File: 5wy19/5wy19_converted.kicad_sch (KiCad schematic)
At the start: 0 parts

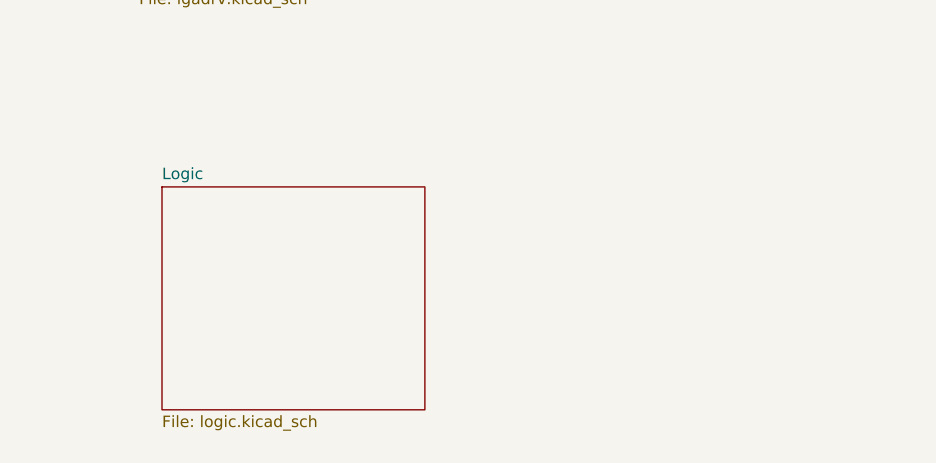
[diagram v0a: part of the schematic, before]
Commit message: Further progress on MCU and connected circuits
Mostly sensors, knock control, some pins from the IO drivers and the unknown AMIS chip
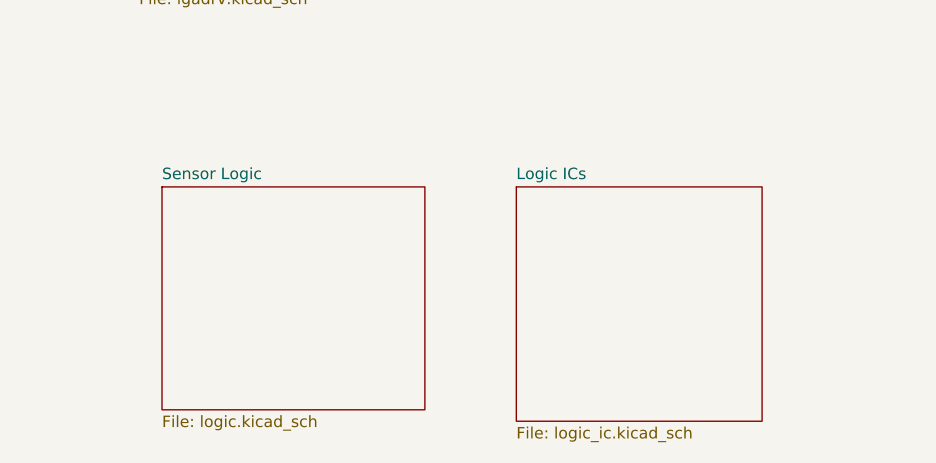
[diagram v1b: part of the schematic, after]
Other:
- sheet Logic renamed Sensor Logic
- added sheet Logic ICs (logic_ic.kicad_sch)
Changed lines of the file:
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@@
+	)
+	(sheet
+		(at 157.48 132.715)
+		(size 27.305 26.035)
+		(exclude_from_sim no)
+		(in_bom yes)
+		(on_board yes)
+		(dnp no)
+		(fields_autoplaced yes)
+		(stroke
+			(width 0.1524)
+			(type solid)
+		)
+		(fill
+			(color 0 0 0 0.0000)
+		)
+		(property "Sheetname" "Logic ICs"
+			(at 157.48 132.0034 0)
+			(effects
+				(font
+					(size 1.27 1.27)
+				)
+				(justify left bottom)
+			)
+		)
+		(property "Sheetfile" "logic_ic.kicad_sch"
+			(at 157.48 159.3346 0)
+			(effects
+				(font
+					(size 1.27 1.27)
+				)
+				(justify left top)
+			)
+		)
+		(instances
+			(project "5wy19_converted"
+				(path "/abd366a8-4ac6-4ee7-9079-ac453affd4f2"
+					(page "11")
+				)
+			)
+		)
 	)
 	(sheet
@@
 			(color 0 0 0 0.0000)
 		)
-		(property "Sheetname" "Logic"
+		(property "Sheetname" "Sensor Logic"
 			(at 118.11 132.0034 0)
 			(effects
@@
 	)
 	(embedded_fonts no)
+	(embedded_files
+		(file
+			(name "a4_sheet.kicad_wks")
+			(type worksheet)
+			(data |KLUv/WCyCWUVAOYdXyEAtxsWHGS5ZWWMnPes1oTrDHxAamZlFGe+cSP//z/UEwFVAE4AWQBZxP/Y
+				I/F/PDdP2uP15E7kfMdDg6XW7M+Dl+TjDQ3Wou2nW37JvwAABASk6L2c1qLiVBd0TkhWnfF32Uf3
+				GDBKKaLO2iO+ZfZRARAQlCESB+y+GyoEkyIKgB9xh7atXWKyolV/yd97OxG29rSmUv7G+52TnrOP
+				GX8f9uxZhT4ceu3h32//fIOjCOeuq/7RRRF/tWuDo2O17dWfuy+rql3sxv88ncVeNEtm8dPFgCH2
+				elqKWjeNdhn5BcOqjiC6zolZiYtS2TAXTcNxZI0tgiJYy7a9FL2wrkRK4zIHR8tgMBuK0Az/zpFz
+				NmX/0b82de6XIpCtTTNTtT09zwsBgYEmEBajliJBrzoRlKNoE9PYkSJuVGvWDSWzTCqNhXVBuMzC
+				aRoEg2HVSigmGUWTbI/7+G7Y/e2ENakm4TYu/MtVCt5+9w/msujgkBqAW9XfiRl3OjsZgIag8Uik
+				nBkSkSRJCh2ARKQEqRu7hKdi4cjAXYATDJrrgiyVqB5BaVnTnmFqzGMhjh02UaDwI+/JDYhkwE1+
+				oiWYGJyVzjshTDD0CinBCdehnAIXCweHmfZh3U/JiARvBhsU+g7YFl/8gApvNEzZR3V5MXUosH5p
+				h5bFEMyCUT+GlyWkxcLPFc9eB/YJLdpa64YJjwaBJlg+SBe/S+6HaTWdhIMO+D3QvmVSTLCcK2b+
+				0XtQwxANMfmhqqTNQi575T6CukIvbbWhQUh3Tn+iQtGbM3hA7o9yj9YD7CxuOVZd9Nof843reekX
+				AiGjJjEdkIkII4RBgfzpkDYl4WVd9Ch/FXjg4AGRGSLFbNFJSmuTchkRQ07niL2UXk1qmpaN9d+x
+				XMRt5KIP6RisKg==|
+			)
+			(checksum "5EDB5D516FD496EB6CB7D2D798AC4F3B")
+		)
+	)
 )

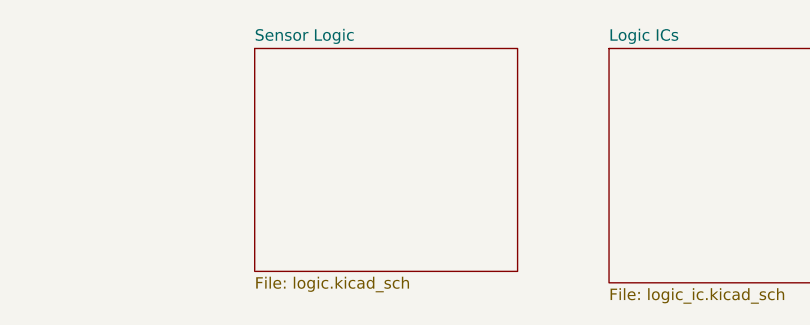
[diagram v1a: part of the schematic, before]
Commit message: Mapped out more pins of MCU and relevant circuits
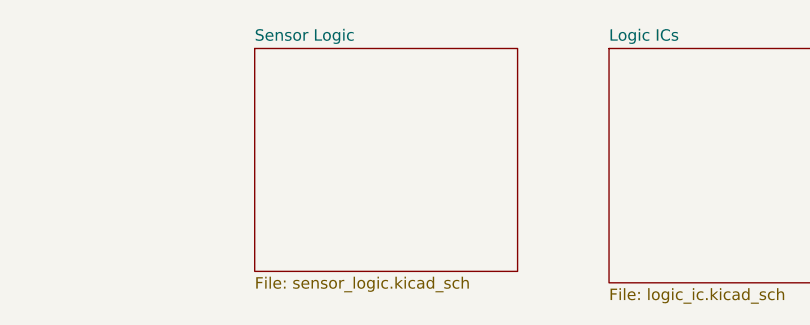
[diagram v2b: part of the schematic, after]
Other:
- sheet Sensor Logic: file logic.kicad_sch -> sensor_logic.kicad_sch
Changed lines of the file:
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@@
 			)
 		)
-		(property "Sheetfile" "logic.kicad_sch"
+		(property "Sheetfile" "sensor_logic.kicad_sch"
 			(at 118.11 158.0646 0)
 			(effects

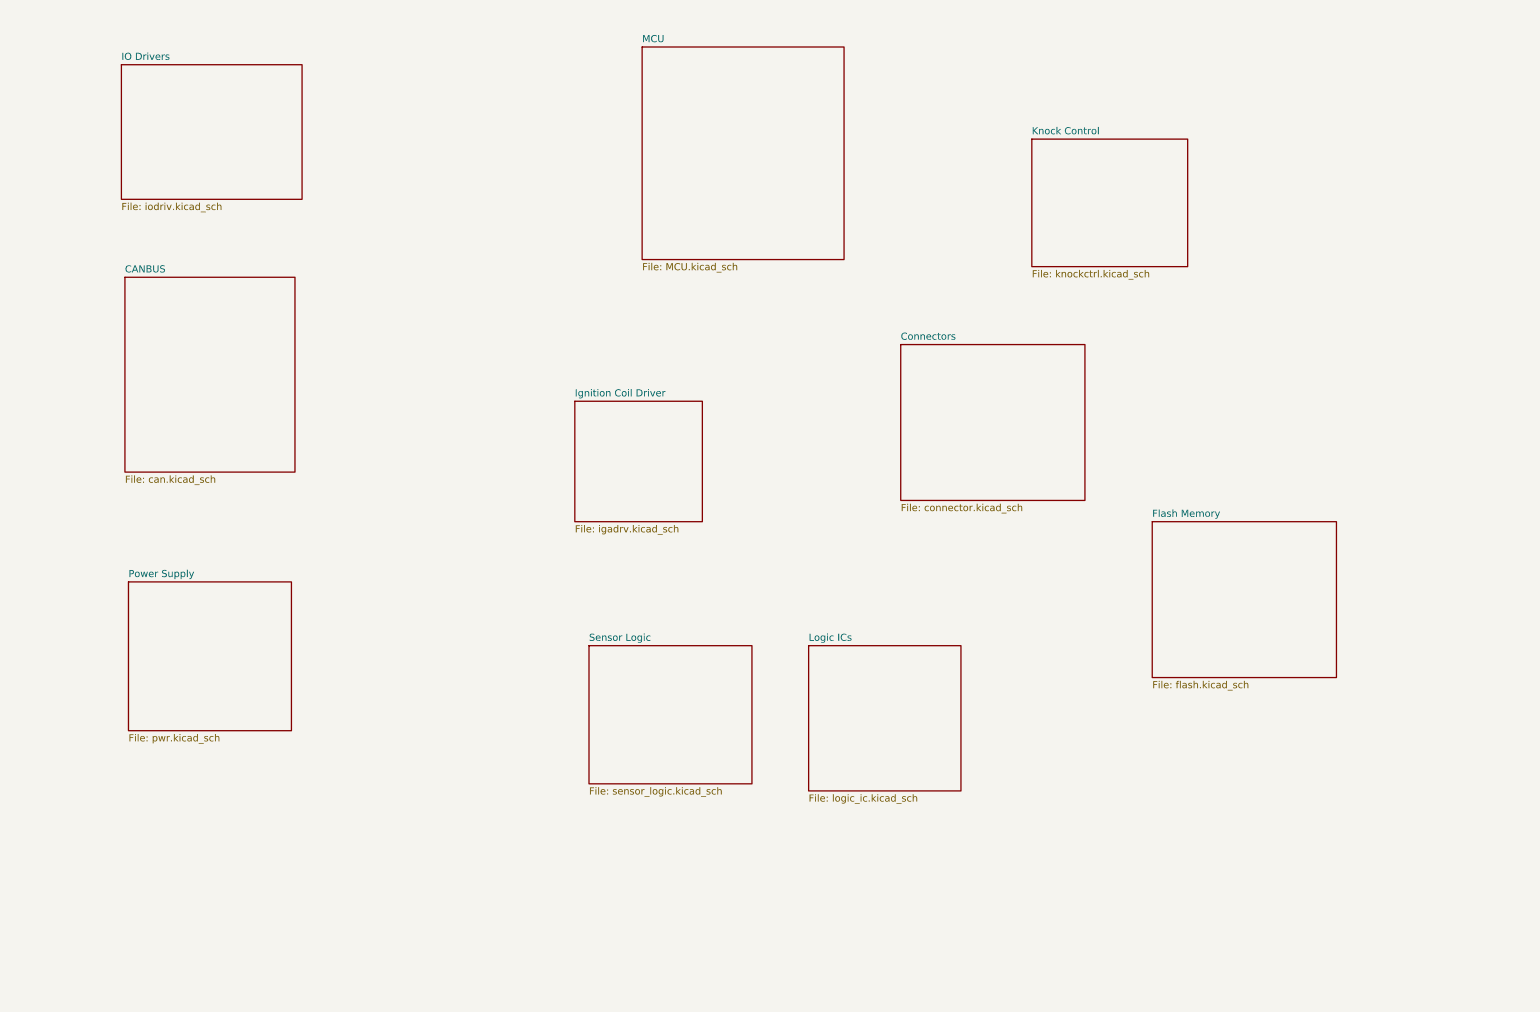
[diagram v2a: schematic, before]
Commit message: Finished most of the subsystems
-- MCU finished
-- Flash finished
-- Power Supply finished
-- I/O Drivers finished
-- CANBUS finished
-- Knock Control finished
-- Connector finished
-- Ignition Driver finished
-- Sensor Logic mostly finished
-- Logic ICs need some work
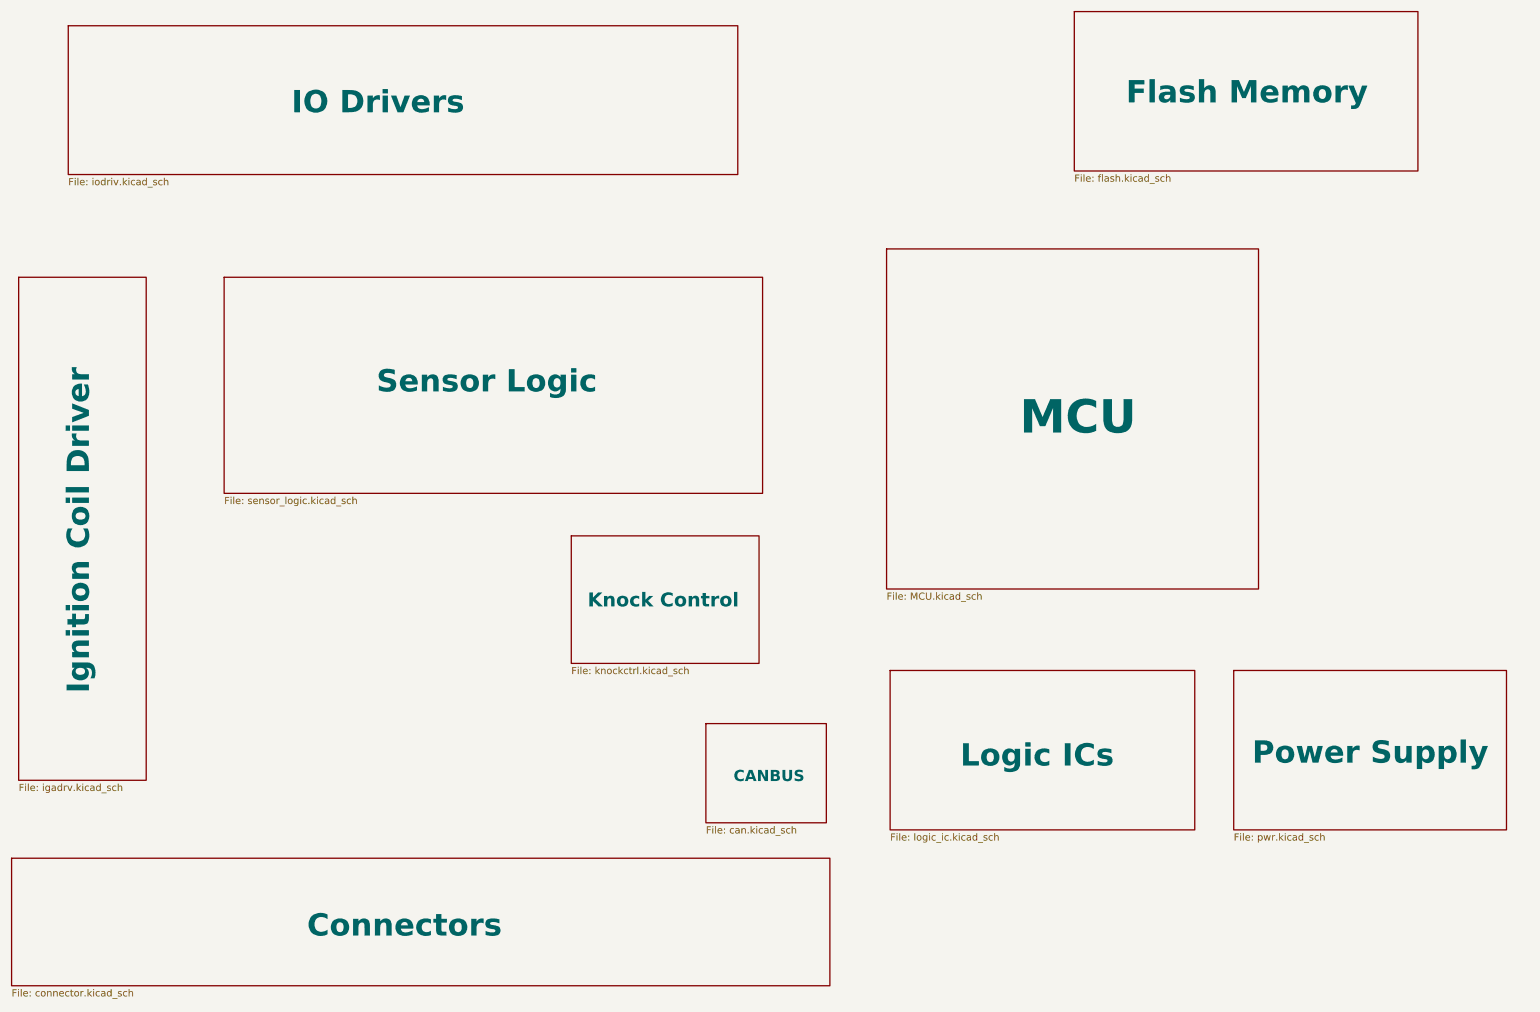
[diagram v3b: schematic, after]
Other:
- title: (none) -> SMIK43 5WY19 Rev. Eng
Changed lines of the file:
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@@
 	(generator_version "9.0")
 	(paper "A4")
-	(sheet
-		(at 219.075 110.49)
-		(size 33.02 27.94)
-		(exclude_from_sim no)
-		(in_bom yes)
-		(on_board yes)
-		(dnp no)
-		(fields_autoplaced yes)
+	(title_block
+		(title "SMIK43 5WY19 Rev. Eng")
+		(date "2025-10-28")
+		(rev "1.0")
+	)
+	(sheet
+		(at 205.105 19.05)
+		(size 61.595 28.575)
+		(exclude_from_sim no)
+		(in_bom yes)
+		(on_board yes)
+		(dnp no)
 		(stroke
 			(width 0.1524)
@@
 		)
 		(property "Sheetname" "Flash Memory"
-			(at 219.075 109.7784 0)
-			(effects
-				(font
-					(size 1.27 1.27)
+			(at 214.376 35.814 0)
+			(effects
+				(font
+					(size 4 4)
+					(thickness 0.8)
+					(bold yes)
 				)
 				(justify left bottom)
@@
 		)
 		(property "Sheetfile" "flash.kicad_sch"
-			(at 219.075 139.0146 0)
+			(at 205.105 48.2096 0)
 			(effects
 				(font
@@
 	)
 	(sheet
-		(at 127.635 25.4)
-		(size 36.195 38.1)
-		(exclude_from_sim no)
-		(in_bom yes)
-		(on_board yes)
-		(dnp no)
-		(fields_autoplaced yes)
+		(at 171.45 61.595)
+		(size 66.675 60.96)
+		(exclude_from_sim no)
+		(in_bom yes)
+		(on_board yes)
+		(dnp no)
 		(stroke
 			(width 0.1524)
@@
 		)
 		(property "Sheetname" "MCU"
-			(at 127.635 24.6884 0)
-			(effects
-				(font
-					(size 1.27 1.27)
+			(at 195.326 95.25 0)
+			(effects
+				(font
+					(size 6 6)
+					(thickness 1.2)
+					(bold yes)
 				)
 				(justify left bottom)
@@
 		)
 		(property "Sheetfile" "MCU.kicad_sch"
-			(at 127.635 64.0846 0)
+			(at 171.45 123.1396 0)
 			(effects
 				(font
@@
 	)
 	(sheet
-		(at 157.48 132.715)
-		(size 27.305 26.035)
-		(exclude_from_sim no)
-		(in_bom yes)
-		(on_board yes)
-		(dnp no)
-		(fields_autoplaced yes)
+		(at 172.085 137.16)
+		(size 54.61 28.575)
+		(exclude_from_sim no)
+		(in_bom yes)
+		(on_board yes)
+		(dnp no)
 		(stroke
 			(width 0.1524)
@@
 		)
 		(property "Sheetname" "Logic ICs"
-			(at 157.48 132.0034 0)
-			(effects
-				(font
-					(size 1.27 1.27)
+			(at 184.658 154.686 0)
+			(effects
+				(font
+					(size 4 4)
+					(thickness 0.8)
+					(bold yes)
 				)
 				(justify left bottom)
@@
 		)
 		(property "Sheetfile" "logic_ic.kicad_sch"
-			(at 157.48 159.3346 0)
+			(at 172.085 166.3196 0)
 			(effects
 				(font
@@
 	)
 	(sheet
-		(at 115.57 88.9)
-		(size 22.86 21.59)
-		(exclude_from_sim no)
-		(in_bom yes)
-		(on_board yes)
-		(dnp no)
-		(fields_autoplaced yes)
+		(at 15.875 66.675)
+		(size 22.86 90.17)
+		(exclude_from_sim no)
+		(in_bom yes)
+		(on_board yes)
+		(dnp no)
 		(stroke
 			(width 0.1524)
@@
 		)
 		(property "Sheetname" "Ignition Coil Driver"
-			(at 115.57 88.1884 0)
-			(effects
-				(font
-					(size 1.27 1.27)
+			(at 28.956 141.224 90)
+			(effects
+				(font
+					(size 4 4)
+					(thickness 0.8)
+					(bold yes)
 				)
 				(justify left bottom)
@@
 		)
 		(property "Sheetfile" "igadrv.kicad_sch"
-			(at 115.57 111.0746 0)
+			(at 15.875 157.4296 0)
 			(effects
 				(font
@@
 	)
 	(sheet
-		(at 118.11 132.715)
-		(size 29.21 24.765)
-		(exclude_from_sim no)
-		(in_bom yes)
-		(on_board yes)
-		(dnp no)
-		(fields_autoplaced yes)
+		(at 52.705 66.675)
+		(size 96.52 38.735)
+		(exclude_from_sim no)
+		(in_bom yes)
+		(on_board yes)
+		(dnp no)
 		(stroke
 			(width 0.1524)
@@
 		)
 		(property "Sheetname" "Sensor Logic"
-			(at 118.11 132.0034 0)
-			(effects
-				(font
-					(size 1.27 1.27)
+			(at 80.01 87.63 0)
+			(effects
+				(font
+					(size 4 4)
+					(thickness 0.8)
+					(bold yes)
 				)
 				(justify left bottom)
@@
 		)
 		(property "Sheetfile" "sensor_logic.kicad_sch"
-			(at 118.11 158.0646 0)
+			(at 52.705 105.9946 0)
 			(effects
 				(font
@@
 	)
 	(sheet
-		(at 197.485 41.91)
-		(size 27.94 22.86)
-		(exclude_from_sim no)
-		(in_bom yes)
-		(on_board yes)
-		(dnp no)
-		(fields_autoplaced yes)
+		(at 114.935 113.03)
+		(size 33.655 22.86)
+		(exclude_from_sim no)
+		(in_bom yes)
+		(on_board yes)
+		(dnp no)
 		(stroke
 			(width 0.1524)
@@
 		)
 		(property "Sheetname" "Knock Control"
-			(at 197.485 41.1984 0)
-			(effects
-				(font
-					(size 1.27 1.27)
+			(at 117.856 125.984 0)
+			(effects
+				(font
+					(size 2.5 2.5)
+					(thickness 0.5)
+					(bold yes)
 				)
 				(justify left bottom)
@@
 		)
 		(property "Sheetfile" "knockctrl.kicad_sch"
-			(at 197.485 65.3546 0)
+			(at 114.935 136.4746 0)
 			(effects
 				(font
@@
 	)
 	(sheet
-		(at 173.99 78.74)
-		(size 33.02 27.94)
-		(exclude_from_sim no)
-		(in_bom yes)
-		(on_board yes)
-		(dnp no)
-		(fields_autoplaced yes)
+		(at 14.605 170.815)
+		(size 146.685 22.86)
+		(exclude_from_sim no)
+		(in_bom yes)
+		(on_board yes)
+		(dnp no)
 		(stroke
 			(width 0.1524)
@@
 		)
 		(property "Sheetname" "Connectors"
-			(at 173.99 78.0284 0)
-			(effects
-				(font
-					(size 1.27 1.27)
+			(at 67.564 185.166 0)
+			(effects
+				(font
+					(size 4 4)
+					(thickness 0.8)
+					(bold yes)
 				)
 				(justify left bottom)
@@
 		)
 		(property "Sheetfile" "connector.kicad_sch"
-			(at 173.99 107.2646 0)
+			(at 14.605 194.2596 0)
 			(effects
 				(font
@@
 	)
 	(sheet
-		(at 34.925 66.675)
-		(size 30.48 34.925)
-		(exclude_from_sim no)
-		(in_bom yes)
-		(on_board yes)
-		(dnp no)
-		(fields_autoplaced yes)
+		(at 139.065 146.685)
+		(size 21.59 17.78)
+		(exclude_from_sim no)
+		(in_bom yes)
+		(on_board yes)
+		(dnp no)
 		(stroke
 			(width 0.1524)
@@
 		)
 		(property "Sheetname" "CANBUS"
-			(at 34.925 65.9634 0)
-			(effects
-				(font
-					(size 1.27 1.27)
+			(at 144.018 157.226 0)
+			(effects
+				(font
+					(size 2 2)
+					(thickness 0.4)
+					(bold yes)
 				)
 				(justify left bottom)
@@
 		)
 		(property "Sheetfile" "can.kicad_sch"
-			(at 34.925 102.1846 0)
+			(at 139.065 165.0496 0)
 			(effects
 				(font
@@
 	)
 	(sheet
-		(at 35.56 121.285)
-		(size 29.21 26.67)
-		(exclude_from_sim no)
-		(in_bom yes)
-		(on_board yes)
-		(dnp no)
-		(fields_autoplaced yes)
+		(at 233.68 137.16)
+		(size 48.895 28.575)
+		(exclude_from_sim no)
+		(in_bom yes)
+		(on_board yes)
+		(dnp no)
 		(stroke
 			(width 0.1524)
@@
 		)
 		(property "Sheetname" "Power Supply"
-			(at 35.56 120.5734 0)
-			(effects
-				(font
-					(size 1.27 1.27)
+			(at 236.982 154.178 0)
+			(effects
+				(font
+					(size 4 4)
+					(thickness 0.8)
+					(bold yes)
 				)
 				(justify left bottom)
@@
 		)
 		(property "Sheetfile" "pwr.kicad_sch"
-			(at 35.56 148.5396 0)
+			(at 233.68 166.3196 0)
 			(effects
 				(font
@@
 	)
 	(sheet
-		(at 34.29 28.575)
-		(size 32.385 24.13)
-		(exclude_from_sim no)
-		(in_bom yes)
-		(on_board yes)
-		(dnp no)
-		(fields_autoplaced yes)
+		(at 24.765 21.59)
+		(size 120.015 26.67)
+		(exclude_from_sim no)
+		(in_bom yes)
+		(on_board yes)
+		(dnp no)
 		(stroke
 			(width 0.1524)
@@
 		)
 		(property "Sheetname" "IO Drivers"
-			(at 34.29 27.8634 0)
-			(effects
-				(font
-					(size 1.27 1.27)
+			(at 64.77 37.592 0)
+			(effects
+				(font
+					(size 4 4)
+					(thickness 0.8)
+					(bold yes)
 				)
 				(justify left bottom)
@@
 		)
 		(property "Sheetfile" "iodriv.kicad_sch"
-			(at 34.29 53.2896 0)
-			(effects
-				(font
+			(at 24.765 48.8446 0)
+			(effects
+				(font
